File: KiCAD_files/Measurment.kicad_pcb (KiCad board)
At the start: 2 copper layers, 21 parts, among them J1 Board_outline, U1 NMA1505SC, U2 AMC1100, U3 AMC1100, U4 AMC1311, U5 NMA1505SC

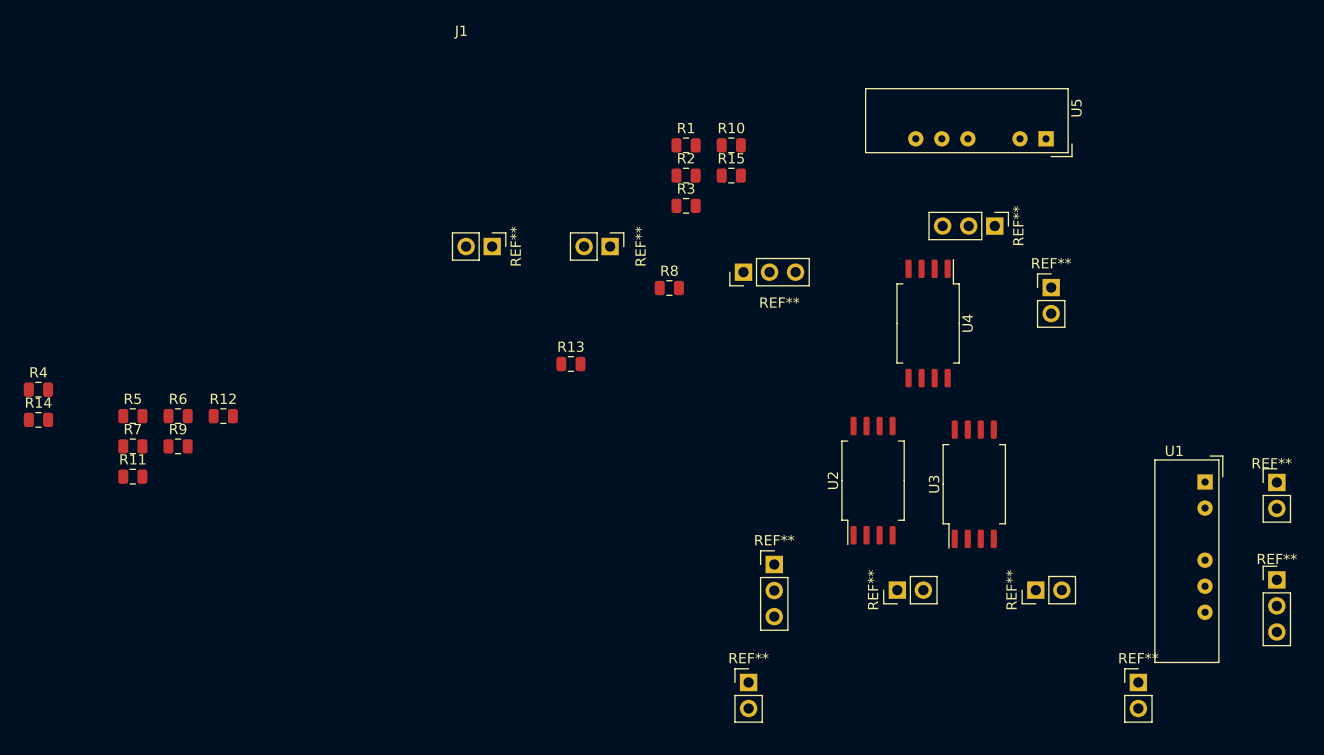
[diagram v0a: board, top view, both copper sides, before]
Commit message: Major modifications of the measurment board schematic Component placement finalized - 3D footprints added - mezzanine assembly on freecad added
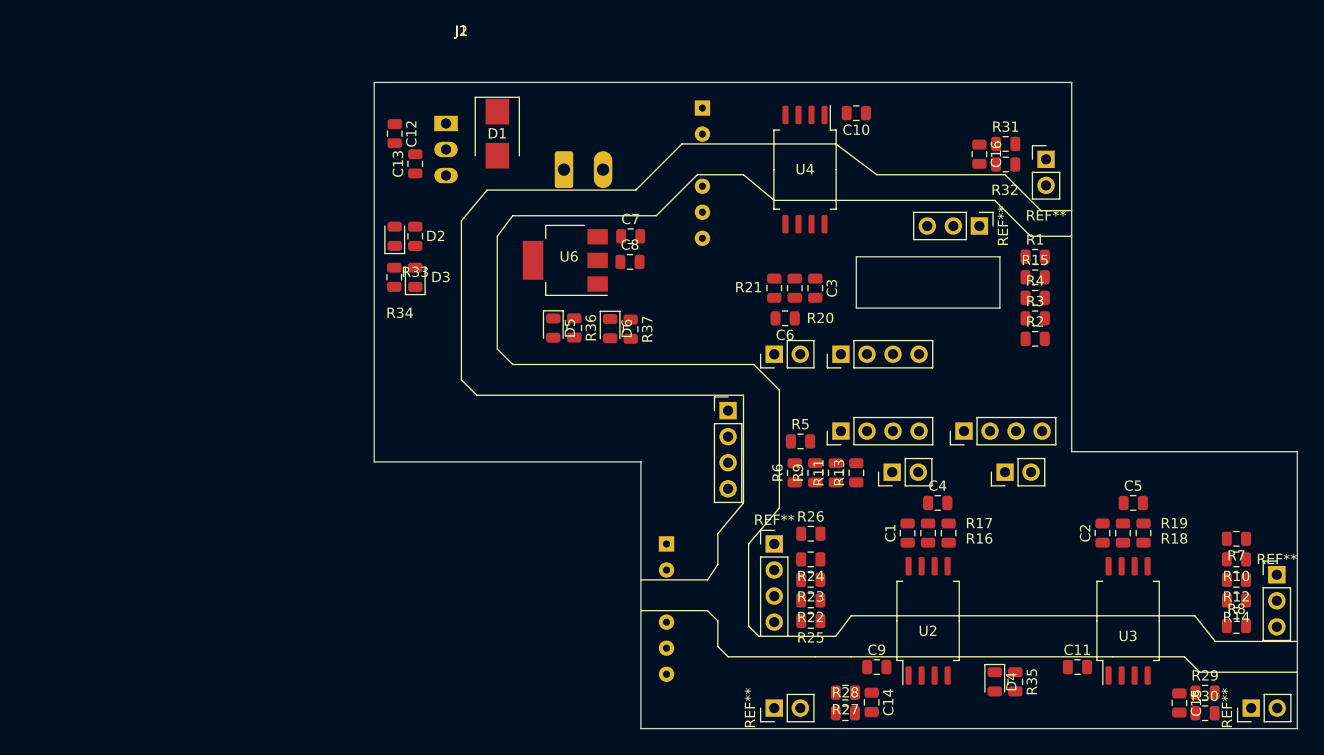
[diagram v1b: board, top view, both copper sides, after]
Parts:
- added C1: C_Small, Capacitor_SMD:C_0805_2012Metric, F.Cu at (83.5, 85.4)
- added C10: C_Small, Capacitor_SMD:C_0805_2012Metric, F.Cu at (78.5, 44.5)
- added C11: C_Small, Capacitor_SMD:C_0805_2012Metric, F.Cu at (100.1, 98.5)
- added C12: C_Small, Capacitor_SMD:C_0805_2012Metric, F.Cu at (33.5, 46.5)
- added C13: C_Small, Capacitor_SMD:C_0805_2012Metric, F.Cu at (35.5, 49.4)
- added C14: C_Small, Capacitor_SMD:C_0805_2012Metric, F.Cu at (80.0, 101.9)
- added C15: C_Small, Capacitor_SMD:C_0805_2012Metric, F.Cu at (110.0, 102.0)
- added C16: C_Small, Capacitor_SMD:C_0805_2012Metric, F.Cu at (90.5, 48.5)
- added C2: C_Small, Capacitor_SMD:C_0805_2012Metric, F.Cu at (102.5, 85.4)
- added C3: C_Small, Capacitor_SMD:C_0805_2012Metric, F.Cu at (74.5, 61.6)
- added C4: C_Small, Capacitor_SMD:C_0805_2012Metric, F.Cu at (86.4, 82.5)
- added C5: C_Small, Capacitor_SMD:C_0805_2012Metric, F.Cu at (105.5, 82.5)
- added C6: C_Small, Capacitor_SMD:C_0805_2012Metric, F.Cu at (71.6, 64.5)
- added C7: C_Small, Capacitor_SMD:C_0805_2012Metric, F.Cu at (56.5, 56.5)
- added C8: C_Small, Capacitor_SMD:C_0805_2012Metric, F.Cu at (56.4, 59.0)
- added C9: C_Small, Capacitor_SMD:C_0805_2012Metric, F.Cu at (80.5, 98.5)
- added D1: D_TVS, Diode_SMD:D_SMB, F.Cu at (43.5, 46.5)
- added D2: LED, LED_SMD:LED_0805_2012Metric, F.Cu at (33.5, 56.5)
- added D3: LED, LED_SMD:LED_0805_2012Metric, F.Cu at (35.5, 60.5)
- added D4: LED, LED_SMD:LED_0805_2012Metric, F.Cu at (92.0, 99.9)
- added D5: LED, LED_SMD:LED_0805_2012Metric, F.Cu at (49.0, 65.5)
- added D6: LED, LED_SMD:LED_0805_2012Metric, F.Cu at (54.5, 65.5)
- added J2: Measurment_stage_outline_signal_inputs, Footprints:Measurment_stage_outline_inputs, F.Cu at (31.5, 41.5)
- added J3: Conn_01x02, Connector_Phoenix_MC:PhoenixContact_MC_1,5_2-G-3.81_1x02_P3.81mm_Horizontal, B.Cu at (50.0, 50.0)
- added R16: R_Small, Resistor_SMD:R_0805_2012Metric, F.Cu at (85.5, 85.4)
- added R17: R_Small, Resistor_SMD:R_0805_2012Metric, F.Cu at (87.5, 85.4)
- added R18: R_Small, Resistor_SMD:R_0805_2012Metric, F.Cu at (104.5, 85.4)
- added R19: R_Small, Resistor_SMD:R_0805_2012Metric, F.Cu at (106.5, 85.4)
- added R20: R_Small, Resistor_SMD:R_0805_2012Metric, F.Cu at (72.5, 61.6)
- added R21: R_Small, Resistor_SMD:R_0805_2012Metric, F.Cu at (70.5, 61.6)
- added R22: R_Small, Resistor_SMD:R_0805_2012Metric, F.Cu at (74.1, 92.0)
- added R23: R_Small, Resistor_SMD:R_0805_2012Metric, F.Cu at (74.1, 90.0)
- added R24: R_Small, Resistor_SMD:R_0805_2012Metric, F.Cu at (74.1, 88.0)
- added R25: R_Small, Resistor_SMD:R_0805_2012Metric, F.Cu at (74.1, 94.0)
- added R26: R_Small, Resistor_SMD:R_0805_2012Metric, F.Cu at (74.1, 85.5)
- added R27: R_Small, Resistor_SMD:R_0805_2012Metric, F.Cu at (77.4, 101.0)
- added R28: R_Small, Resistor_SMD:R_0805_2012Metric, F.Cu at (77.4, 103.0)
- added R29: R_Small, Resistor_SMD:R_0805_2012Metric, F.Cu at (112.5, 101.0)
- added R30: R_Small, Resistor_SMD:R_0805_2012Metric, F.Cu at (112.5, 103.0)
- added R31: R_Small, Resistor_SMD:R_0805_2012Metric, F.Cu at (93.1, 47.5)
- added R32: R_Small, Resistor_SMD:R_0805_2012Metric, F.Cu at (93.1, 49.5)
- added R33: R_Small, Resistor_SMD:R_0805_2012Metric, F.Cu at (35.5, 56.5)
- added R34: R_Small, Resistor_SMD:R_0805_2012Metric, F.Cu at (33.5, 60.5)
- added R35: R_Small, Resistor_SMD:R_0805_2012Metric, F.Cu at (94.0, 99.9)
- added R36: R_Small, Resistor_SMD:R_0805_2012Metric, F.Cu at (51.0, 65.4)
- added R37: R_Small, Resistor_SMD:R_0805_2012Metric, F.Cu at (56.5, 65.6)
- added U6: AMS1117-3.3, Package_TO_SOT_SMD:SOT-223-3_TabPin2, F.Cu at (50.1, 58.9)
- added U7: NMA1505SC, Converter_DCDC:Converter_DCDC_muRata_NMAxxxxSC_THT, B.Cu at (63.5, 44.0)
- J1: value Board_outline -> Measurment_stage_outline_outputs; footprint Footprints:Board outline -> Footprints:Measurment_stage_outline_outputs
- U1: moved to B.Cu
- U5: value NMA1505SC -> R-78C5.0-1.0; footprint Converter_DCDC:Converter_DCDC_muRata_NMAxxxxSC_THT -> Converter_DCDC:Converter_DCDC_RECOM_R-78E-0.5_THT; moved to B.Cu
- moved R14 118.1 mm to (115.6, 92.0), turned to 180 degrees
- moved R7 108.0 mm to (115.6, 86.0), turned to 180 degrees
- moved R12 100.1 mm to (115.6, 90.0), turned to 180 degrees
- moved R4 97.6 mm to (95.9, 62.5)
- moved R11 68.5 mm to (76.5, 79.6), turned to 90 degrees
- moved R5 65.1 mm to (73.1, 76.5)
- moved R8 64.4 mm to (115.6, 94.5)
- moved R10 63.7 mm to (115.6, 88.0), turned to 180 degrees
- moved R9 62.2 mm to (74.5, 79.6), turned to 90 degrees
- moved R6 60.4 mm to (72.5, 79.6), turned to 90 degrees
- moved U5 58.5 mm to (38.5, 45.5)
- moved U1 52.8 mm to (60.0, 86.5), turned to 180 degrees
- moved R2 37.6 mm to (95.9, 66.5)
- moved R3 35.8 mm to (95.9, 64.5)
- moved R1 35.7 mm to (95.9, 58.5)
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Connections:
- J1 pad 1: +5VD -> +15V
- J1 pad 10: /VIHigh+ -> /IILow2_ADC
- J1 pad 11: GNDREF -> /IIHigh_ADC
- J1 pad 12: /VILow1+ -> /VTh_ADC
- J1 pad 13: /VILow1- -> +3V3
- J1 pad 14: /VILow2+ -> GNDD
- J1 pad 15: /VILow2- -> +5VD
- J1 pad 2: /IILow1 -> GNDREF
- J1 pad 3: GNDD -> /VILow1+_ADC
- J1 pad 4: +5VD -> /VILow1-_ADC
- J1 pad 5: /IILow2 -> /VILow2+_ADC
- J1 pad 6: GNDD -> /VILow2_ADC
- J1 pad 7: +5VD -> /VIHigh+_ADC
- J1 pad 8: /IIHigh -> /VIHigh-_ADC
- J1 pad 9: GNDD -> /IILow1_ADC
- U1 pad 1: +15V -> +5V
- U2 pad 2: /VILow1+ -> Net-(C14-Pad1)
- U2 pad 3: /VILow1- -> Net-(C14-Pad2)
- U3 pad 2: /VILow2+ -> Net-(C15-Pad1)
- U3 pad 3: /VILow2- -> Net-(C15-Pad2)
- U4 pad 2: /VIHigh+ -> Net-(C16-Pad1)
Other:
- board outline added: 90 x 63 mm
